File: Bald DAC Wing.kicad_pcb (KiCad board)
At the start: 2 copper layers, 51 parts, among them J1 XTRA, J2 DAC_A_Out, J3 DAC_B_Out, J5 Z_Out, U1 AD5447, U2 AD8065ARTZ, U3 AD8065ARTZ, U4 74LVC574APWR, U5 74LVC574APWR, U6 74LVC1G04, U7 REF3425

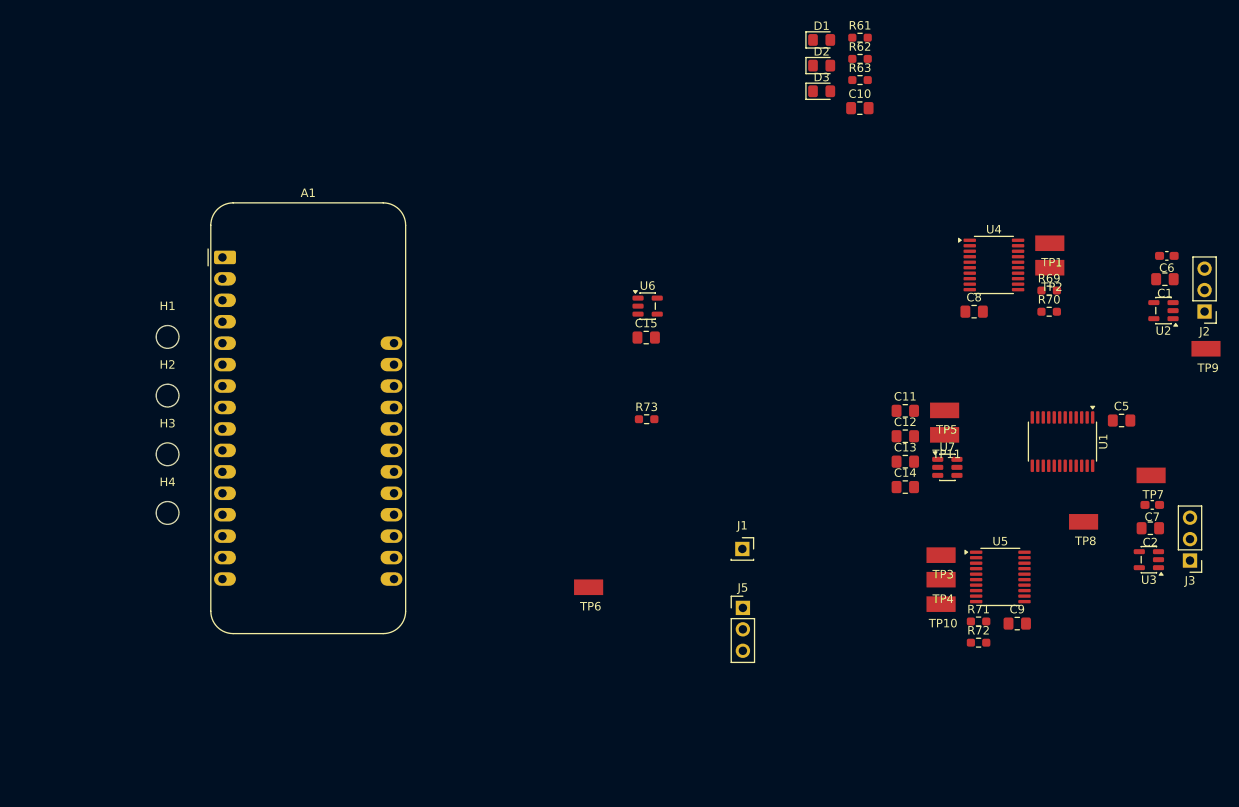
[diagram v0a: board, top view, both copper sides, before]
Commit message: only use 1/2 the feather!
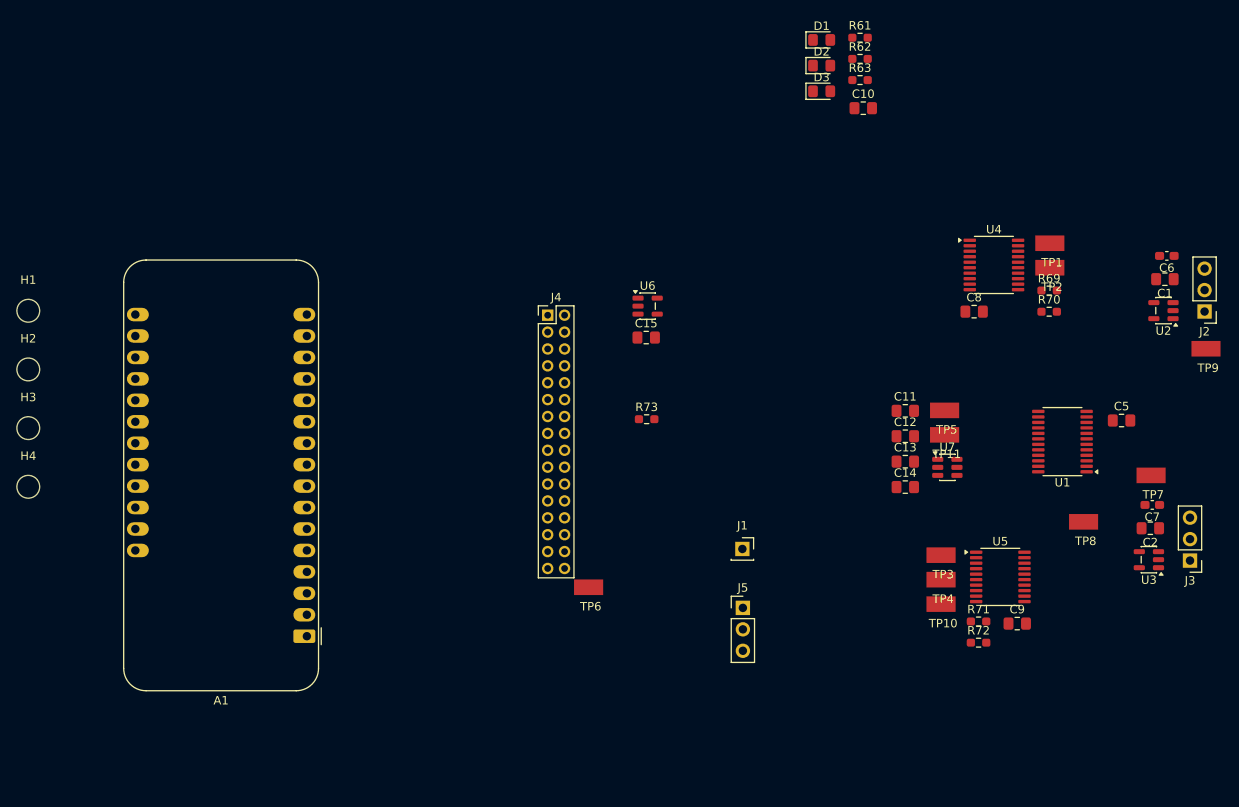
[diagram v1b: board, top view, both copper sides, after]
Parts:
- added J4: Data Debug HDR, Connector_PinHeader_2.00mm:PinHeader_2x16_P2.00mm_Vertical, F.Cu at (119.5, 72.5)
- moved A1 46.0 mm to (91.0, 110.5), turned to 180 degrees
- moved H4 16.8 mm to (58.0, 92.8)
- moved H1 16.8 mm to (58.0, 72.0)
- moved H2 16.8 mm to (58.0, 79.0)
- moved H3 16.8 mm to (58.0, 85.9)
- moved C10 0.41 mm to (156.9, 48.0)
- turned U1 to 180 degrees
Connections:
- A1 pad 10: unconnected-(A1-A5-Pad10) -> /D5
- A1 pad 14: /Z_Blank -> /DAC_AB
- A1 pad 15: unconnected-(A1-TX-Pad15) -> /LCLKL
- A1 pad 16: /DAC_AB -> /Z_Blank
- A1 pad 19: /D0 -> unconnected-(A1-D0-Pad19)
- A1 pad 20: /D1 -> unconnected-(A1-D1-Pad20)
- A1 pad 21: /D2 -> unconnected-(A1-D2-Pad21)
- A1 pad 22: /D3 -> unconnected-(A1-D3-Pad22)
- A1 pad 23: /D4 -> unconnected-(A1-D4-Pad23)
- A1 pad 24: /D5 -> unconnected-(A1-D5-Pad24)
- A1 pad 25: /LCLKL -> unconnected-(A1-D6-Pad25)
- A1 pad 5: unconnected-(A1-A0-Pad5) -> /D0
- A1 pad 6: unconnected-(A1-A1-Pad6) -> /D1
- A1 pad 7: unconnected-(A1-A2-Pad7) -> /D2
- A1 pad 8: unconnected-(A1-A3-Pad8) -> /D3
- A1 pad 9: unconnected-(A1-A4-Pad9) -> /D4
- C10 pad 1: (no net) -> +3V3
- C10 pad 2: (no net) -> GND

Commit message: applied 4-layer DRC for OSH Park
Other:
- copper layers 2 -> 4
- rule pad_to_mask_clearance: 0 -> 0.051
- board text added: "3V3"
- board text added: "AREF"
- board text added: "CS"
- board text added: "D0"
- board text added: "D1"
- board text added: "D2"
- board text added: "D3"
- board text added: "D4"
- board text added: "D5"
- board text added: "DAC_AB"
- board text added: "GND"
- board text added: "LCLKL"
- board text added: "LOE"
- board text added: "REF_EN"
- board text added: "Z_Blank"
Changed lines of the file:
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@@
 	(layers
 		(0 "F.Cu" signal)
+		(4 "In1.Cu" power "In1.Gnd.Cu")
+		(6 "In2.Cu" power "In2.3v3.Cu")
 		(2 "B.Cu" signal)
 		(9 "F.Adhes" user "F.Adhesive")
@@
 		(35 "F.Fab" user)
 		(33 "B.Fab" user)
-		(39 "User.1" user)
-		(41 "User.2" user)
-		(43 "User.3" user)
-		(45 "User.4" user)
 	)
 	(setup
-		(pad_to_mask_clearance 0)
+		(stackup
+			(layer "F.SilkS"
+				(type "Top Silk Screen")
+				(color "White")
+			)
+			(layer "F.Paste"
+				(type "Top Solder Paste")
+			)
+			(layer "F.Mask"
+				(type "Top Solder Mask")
+				(color "Red")
+				(thickness 0.01)
+			)
+			(layer "F.Cu"
+				(type "copper")
+				(thickness 0.035)
+			)
+			(layer "dielectric 1"
+				(type "core")
+				(thickness 0.48)
+				(material "FR4")
+				(epsilon_r 4.5)
+				(loss_tangent 0.02)
+			)
+			(layer "In1.Cu"
+				(type "copper")
+				(thickness 0.035)
+			)
+			(layer "dielectric 2"
+				(type "prepreg")
+				(thickness 0.48)
+				(material "FR4")
+				(epsilon_r 4.5)
+				(loss_tangent 0.02)
+			)
+			(layer "In2.Cu"
+				(type "copper")
+				(thickness 0.035)
+			)
+			(layer "dielectric 3"
+				(type "core")
+				(thickness 0.48)
+				(material "FR4")
+				(epsilon_r 4.5)
+				(loss_tangent 0.02)
+			)
+			(layer "B.Cu"
+				(type "copper")
+				(thickness 0.035)
+			)
+			(layer "B.Mask"
+				(type "Bottom Solder Mask")
+				(color "Red")
+				(thickness 0.01)
+			)
+			(layer "B.Paste"
+				(type "Bottom Solder Paste")
+			)
+			(layer "B.SilkS"
+				(type "Bottom Silk Screen")
+				(color "White")
+			)
+			(copper_finish "None")
+			(dielectric_constraints no)
+		)
+		(pad_to_mask_clearance 0.051)
+		(solder_mask_min_width 0.1524)
 		(allow_soldermask_bridges_in_footprints no)
 		(tenting
@@
 		(capping no)
 		(filling no)
+		(zone_defaults)
 		(pcbplotparams
 			(layerselection 0x00000000_00000000_55555555_5755f5ff)
@@
 			)
 		)
+	)
+	(gr_text "Z_Blank"
+		(at 94.3 72.45 0)
+		(layer "F.SilkS")
+		(effects
+			(font
+				(size 0.8 0.8)
+				(thickness 0.12)
+			)
+		)
+	)
+	(gr_text "LCLKL"
+		(at 94.3 74.99 0)
+		(layer "F.SilkS")
+		(effects
+			(font
+				(size 0.8 0.8)
+				(thickness 0.12)
+			)
+		)
+	)
+	(gr_text "DAC_AB"
+		(at 94.3 77.53 0)
+		(layer "F.SilkS")
+		(effects
+			(font
+				(size 0.8 0.8)
+				(thickness 0.12)
+			)
+		)
+	)
+	(gr_text "REF_EN"
+		(at 94.3 80.07 0)
+		(layer "F.SilkS")
+		(effects
+			(font
+				(size 0.8 0.8)
+				(thickness 0.12)
+			)
+		)
+	)
+	(gr_text "LOE"
+		(at 94.3 82.61 0)
+		(layer "F.SilkS")
+		(effects
+			(font
+				(size 0.8 0.8)
+				(thickness 0.12)
+			)
+		)
+	)
+	(gr_text "CS"
+		(at 94.3 85.15 0)
+		(layer "F.SilkS")
+		(effects
+			(font
+				(size 0.8 0.8)
+				(thickness 0.12)
+			)
+		)
+	)
+	(gr_text "D5"
+		(at 94.3 87.69 0)
+		(layer "F.SilkS")
+		(effects
+			(font
+				(size 0.8 0.8)
+				(thickness 0.12)
+			)
+		)
+	)
+	(gr_text "D4"
+		(at 94.3 90.23 0)
+		(layer "F.SilkS")
+		(effects
+			(font
+				(size 0.8 0.8)
+				(thickness 0.12)
+			)
+		)
+	)
+	(gr_text "D3"
+		(at 94.3 92.77 0)
+		(layer "F.SilkS")
+		(effects
+			(font
+				(size 0.8 0.8)
+				(thickness 0.12)
+			)
+		)
+	)
+	(gr_text "D2"
+		(at 94.3 95.31 0)
+		(layer "F.SilkS")
+		(effects
+			(font
+				(size 0.8 0.8)
+				(thickness 0.12)
+			)
+		)
+	)
+	(gr_text "D1"
+		(at 94.3 97.85 0)
+		(layer "F.SilkS")
+		(effects
+			(font
+				(size 0.8 0.8)
+				(thickness 0.12)
+			)
+		)
+	)
+	(gr_text "D0"
+		(at 94.3 100.39 0)
+		(layer "F.SilkS")
+		(effects
+			(font
+				(size 0.8 0.8)
+				(thickness 0.12)
+			)
+		)
+	)
+	(gr_text "GND"
+		(at 94.3 102.93 0)
+		(layer "F.SilkS")
+		(effects
+			(font
+				(size 0.8 0.8)
+				(thickness 0.12)
+			)
+		)
+	)
+	(gr_text "AREF"
+		(at 94.3 105.47 0)
+		(layer "F.SilkS")
+		(effects
+			(font
+				(size 0.8 0.8)
+				(thickness 0.12)
+			)
+		)
+	)
+	(gr_text "3V3"
+		(at 94.3 108.01 0)
+		(layer "F.SilkS")
+		(effects
+			(font
+				(size 0.8 0.8)
+				(thickness 0.12)
+			)
+		)

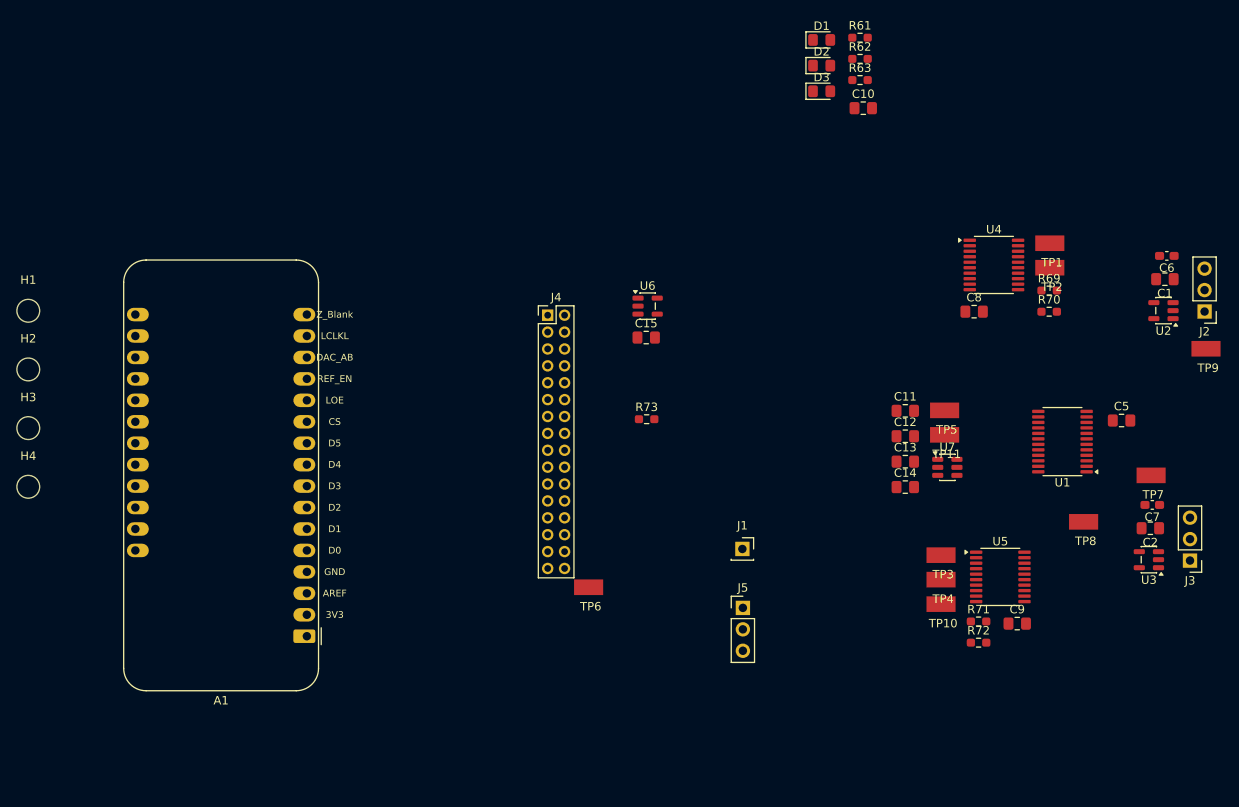
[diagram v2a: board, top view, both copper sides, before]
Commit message: got rid of the switches
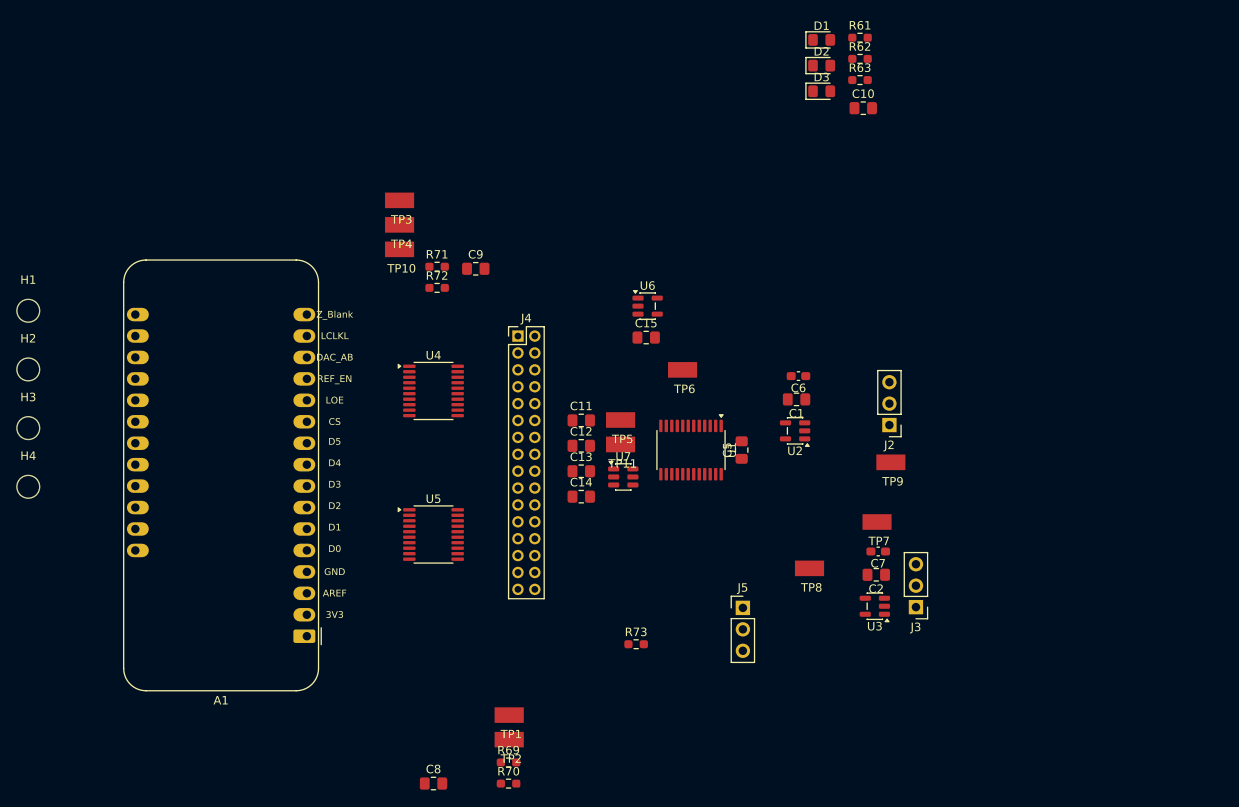
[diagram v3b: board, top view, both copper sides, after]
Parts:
- removed J1: XTRA, Connector_PinSocket_2.54mm:PinSocket_1x01_P2.54mm_Vertical
- moved R69 85.0 mm to (114.9, 125.5)
- moved R70 85.0 mm to (114.9, 128.0)
- moved C8 85.0 mm to (106.0, 128.0)
- moved TP1 85.0 mm to (115.0, 119.9)
- moved TP2 85.0 mm to (115.0, 122.8)
- moved C9 76.7 mm to (111.0, 67.0)
- moved R71 76.7 mm to (106.4, 66.8)
- moved TP10 76.7 mm to (102.0, 64.7)
- moved TP3 76.7 mm to (102.0, 58.9)
- moved R72 76.7 mm to (106.4, 69.3)
- moved TP4 76.7 mm to (102.0, 61.8)
- moved U4 68.0 mm to (106.0, 81.5)
- moved U5 67.3 mm to (106.0, 98.5)
- moved C6 45.9 mm to (149.2, 79.7)
- moved C1 45.9 mm to (149.0, 82.5)
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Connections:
- A1 pad 1: Net-(A1-~{RESET}) -> unconnected-(A1-~{RESET}-Pad1)
- R69 pad 2: Net-(U4-D7) -> Net-(U4-D1)
- R70 pad 2: Net-(U4-D6) -> Net-(U4-D0)
- TP1 pad 1: Net-(U4-Q6) -> Net-(U4-Q0)
- TP2 pad 1: Net-(U4-Q7) -> Net-(U4-Q1)
- U4 pad 12: Net-(U4-Q7) -> /DB6
- U4 pad 13: Net-(U4-Q6) -> /DB7
- U4 pad 14: /DB6 -> /DB8
- U4 pad 15: /DB7 -> /DB9
- U4 pad 16: /DB8 -> /DB10
- U4 pad 17: /DB9 -> /DB11
- U4 pad 18: /DB10 -> Net-(U4-Q1)
- U4 pad 19: /DB11 -> Net-(U4-Q0)
- U4 pad 2: /D0 -> Net-(U4-D0)
- U4 pad 3: /D1 -> Net-(U4-D1)
- U4 pad 4: /D2 -> /D5
- U4 pad 5: /D3 -> /D4
- U4 pad 6: /D4 -> /D3
- U4 pad 7: /D5 -> /D2
- U4 pad 8: Net-(U4-D6) -> /D1
- U4 pad 9: Net-(U4-D7) -> /D0
- U5 pad 2: /D0 -> /D5
- U5 pad 3: /D1 -> /D4
- U5 pad 4: /D2 -> /D3
- U5 pad 5: /D3 -> /D2
- U5 pad 6: /D4 -> /D1
- U5 pad 7: /D5 -> /D0

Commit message: added power header
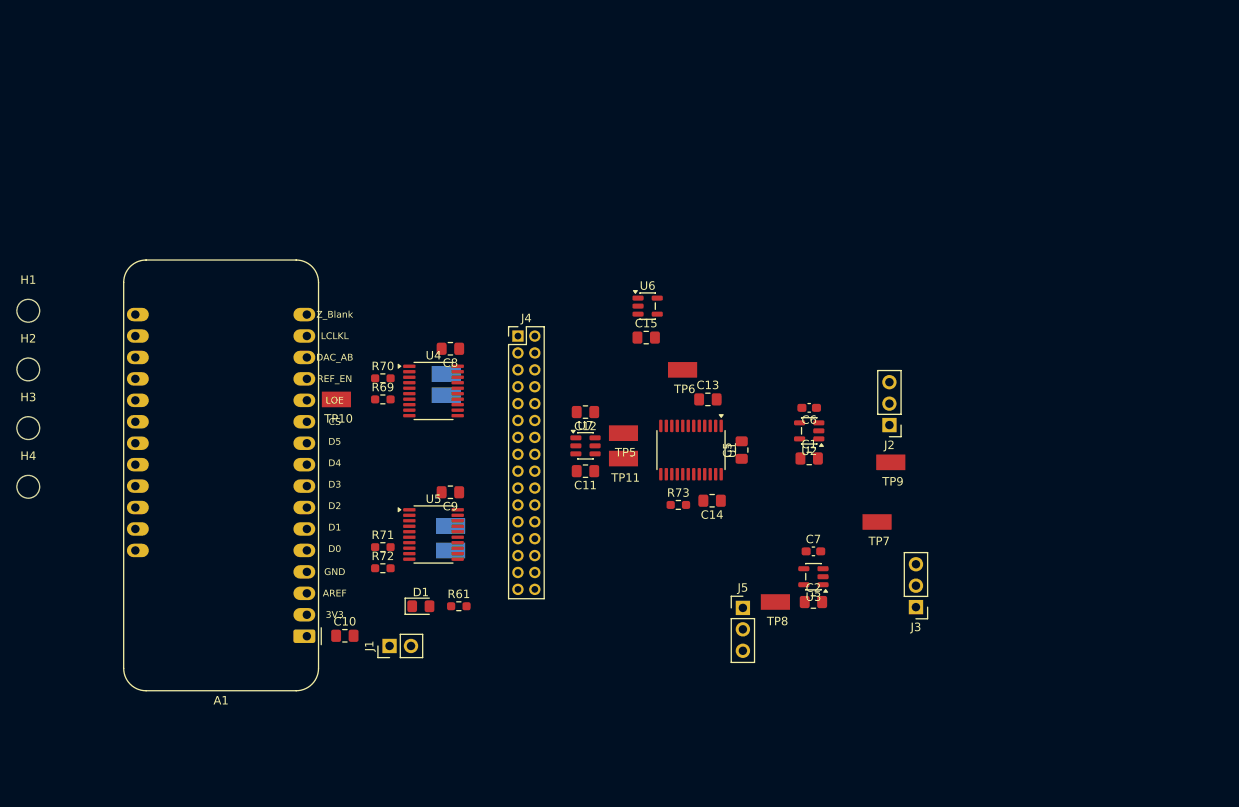
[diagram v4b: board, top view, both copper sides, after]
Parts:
- removed D2: PwrB+, LED_SMD:LED_0805_2012Metric_Pad1.15x1.40mm_HandSolder
- removed D3: Vusb, LED_SMD:LED_0805_2012Metric_Pad1.15x1.40mm_HandSolder
- removed R62, R63: 1k, Resistor_SMD:R_0603_1608Metric_Pad0.98x0.95mm_HandSolder
- added J1: PWR, Connector_PinHeader_2.54mm:PinHeader_1x02_P2.54mm_Vertical, F.Cu at (100.8, 111.7)
- TP1, TP2, TP3, TP4: moved to B.Cu
- moved C10 87.6 mm to (95.5, 110.5)
- moved R61 82.4 mm to (109.0, 107.0)
- moved D1 82.2 mm to (104.5, 107.0)
- moved C8 51.5 mm to (108.0, 76.5), turned to 180 degrees
- moved R70 50.3 mm to (100.0, 80.0)
- moved R69 45.5 mm to (100.0, 82.5)
- moved TP2 41.5 mm to (107.5, 82.0), turned to 180 degrees
- moved TP1 41.1 mm to (107.5, 79.5), turned to 180 degrees
- moved TP3 39.0 mm to (108.0, 97.5), turned to 180 degrees
- moved TP4 39.0 mm to (108.0, 100.4), turned to 180 degrees
- moved R71 33.8 mm to (100.0, 100.0)
- moved R72 33.8 mm to (100.0, 102.5)
- moved C9 26.6 mm to (108.0, 93.5), turned to 180 degrees
- moved TP10 19.3 mm to (94.5, 82.5)
- moved C13 17.2 mm to (138.5, 82.5)
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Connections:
- A1 pad 2: +3V3 -> Net-(A1-3V3)
- A1 pad 26: Vusb -> unconnected-(A1-USB-Pad26)
- J4 pad 31: unconnected-(J4-Pin_31-Pad31) -> GND

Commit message: first edge cut layer
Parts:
- added TP12: TestPoint_Harwin, My Libraries:Harwin-S1751-46-Test-Point, F.Cu at (108.0, 103.5)
- added TP13: TestPoint_Harwin, My Libraries:Harwin-S1751-46-Test-Point, F.Cu at (108.0, 86.5)
- C13, C14: footprint Capacitor_SMD:C_0805_2012Metric_Pad1.18x1.45mm_HandSolder -> Capacitor_SMD:C_0402_1005Metric_Pad0.74x0.62mm_HandSolder
- moved U6 32.9 mm to (104.5, 90.5)
- moved J5 32.5 mm to (147.0, 75.0)
- moved C15 27.0 mm to (109.0, 90.5), turned to -90 degrees
- moved TP9 18.8 mm to (142.5, 83.5)
- moved C1 18.5 mm to (135.2, 79.0), turned to -90 degrees
- moved J3 17.8 mm to (147.0, 99.5)
- moved C2 16.2 mm to (136.0, 100.5), turned to -90 degrees
- moved TP7 16.1 mm to (142.5, 95.5)
- moved U2 14.0 mm to (138.5, 79.0), turned to 90 degrees
- moved J2 13.6 mm to (147.0, 89.5)
- moved U3 12.4 mm to (139.0, 100.5), turned to 90 degrees
- moved C6 10.3 mm to (141.2, 79.0), turned to 90 degrees
- moved C7 9.00 mm to (142.0, 100.5), turned to -90 degrees
- moved TP6 7.83 mm to (142.5, 75.5), turned to 180 degrees
- moved J1 6.69 mm to (95.2, 108.0)
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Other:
- board outline added: 63 x 45 mm

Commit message: 1st rough layout
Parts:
- moved H4 81.2 mm to (137.0, 111.5)
- moved H1 79.0 mm to (137.0, 71.0)
- moved H3 46.2 mm to (96.5, 111.5)
- moved H2 39.3 mm to (96.5, 71.0)
- moved C12 26.0 mm to (121.0, 111.0), turned to -90 degrees
- moved TP5 25.0 mm to (118.5, 111.0), turned to 90 degrees
- moved U7 22.1 mm to (125.0, 111.0), turned to 90 degrees
- moved TP11 20.8 mm to (130.5, 111.0), turned to 90 degrees
- moved C11 19.8 mm to (128.0, 111.0), turned to -90 degrees
- moved TP8 19.1 mm to (124.0, 102.0)
- moved C6 18.2 mm to (123.3, 82.0), turned to -90 degrees
- moved TP6 16.8 mm to (126.0, 78.5), turned to 0 degrees
- moved C2 15.8 mm to (121.0, 105.5)
- moved C7 15.8 mm to (127.0, 105.5)
- moved U3 15.8 mm to (124.0, 105.5)
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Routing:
- net /D0: track 0.00 -> 34.5 mm, vias 0 -> 1
- net /D1: track 0.00 -> 32.6 mm, vias 0 -> 1
- net /D2: track 0.00 -> 32.1 mm, vias 0 -> 1
- net /D4: track 0.00 -> 30.9 mm, vias 0 -> 1
- net /D3: track 0.00 -> 30.9 mm, vias 0 -> 1
- net /D5: track 0.00 -> 30.8 mm, vias 0 -> 1
- net /DB11: track 0.00 -> 27.0 mm
- net /DB10: track 0.00 -> 25.1 mm
- net /DB9: track 0.00 -> 21.9 mm
- net /DB5: track 0.00 -> 21.4 mm
- net /DB4: track 0.00 -> 21.3 mm
- net /DB3: track 0.00 -> 20.0 mm
- net /DB8: track 0.00 -> 19.3 mm
- net /DB2: track 0.00 -> 18.8 mm
- net /DB7: track 0.00 -> 17.6 mm
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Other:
- board size 63 x 45 mm -> 52 x 46.5 mm
